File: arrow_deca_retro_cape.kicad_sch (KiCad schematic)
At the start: 26 parts, among them J1 ZXSP_ED2X28_SPE_SOL_EDGE, J10 Conn_02x05_Odd_Even, J12 Conn_01x03, J13 Conn_01x01, J14 Conn_01x02, J15 Conn_01x03, J16 Conn_01x06, J2 Conn_01x03, J4 DB9_Male, J5 DINC_MIN_TM_6_1, J6 Conn_02x20_Odd_Even, J7 Conn_01x03, J8 P8_Male, J9 P9_Male, U4 LM1117-3.3, U5 LM1117-2.5

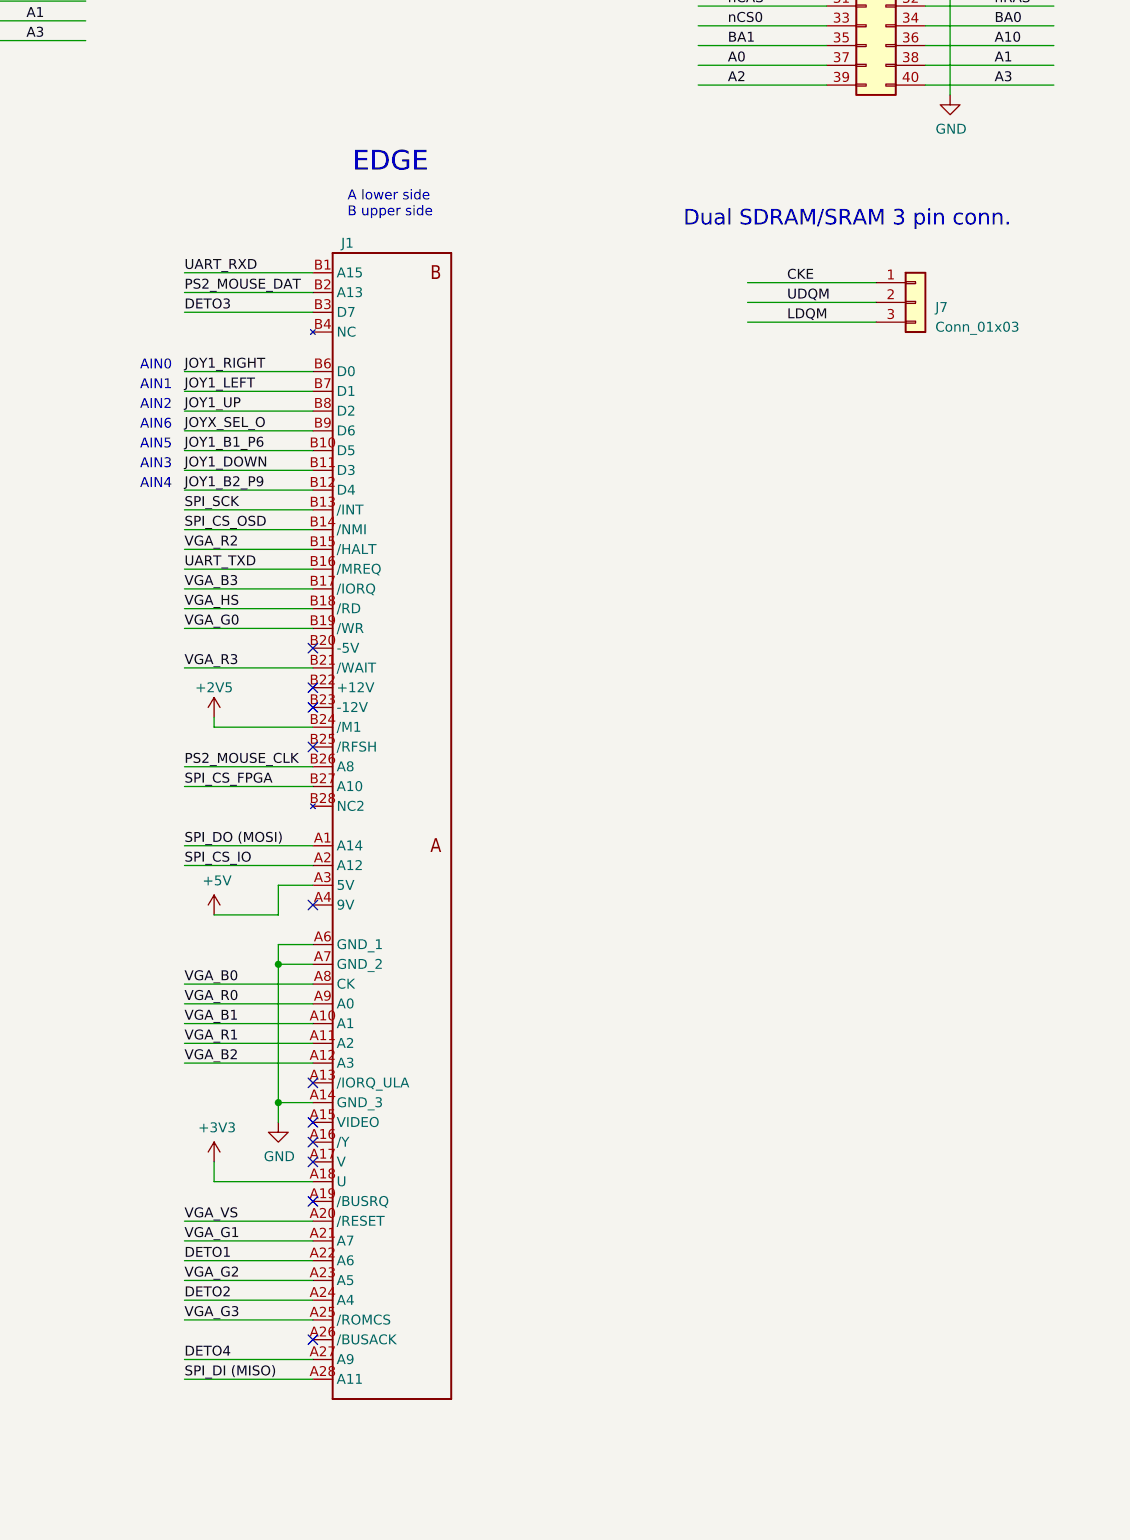
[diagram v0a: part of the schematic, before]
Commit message: v0.61 2-layer. Edge removed
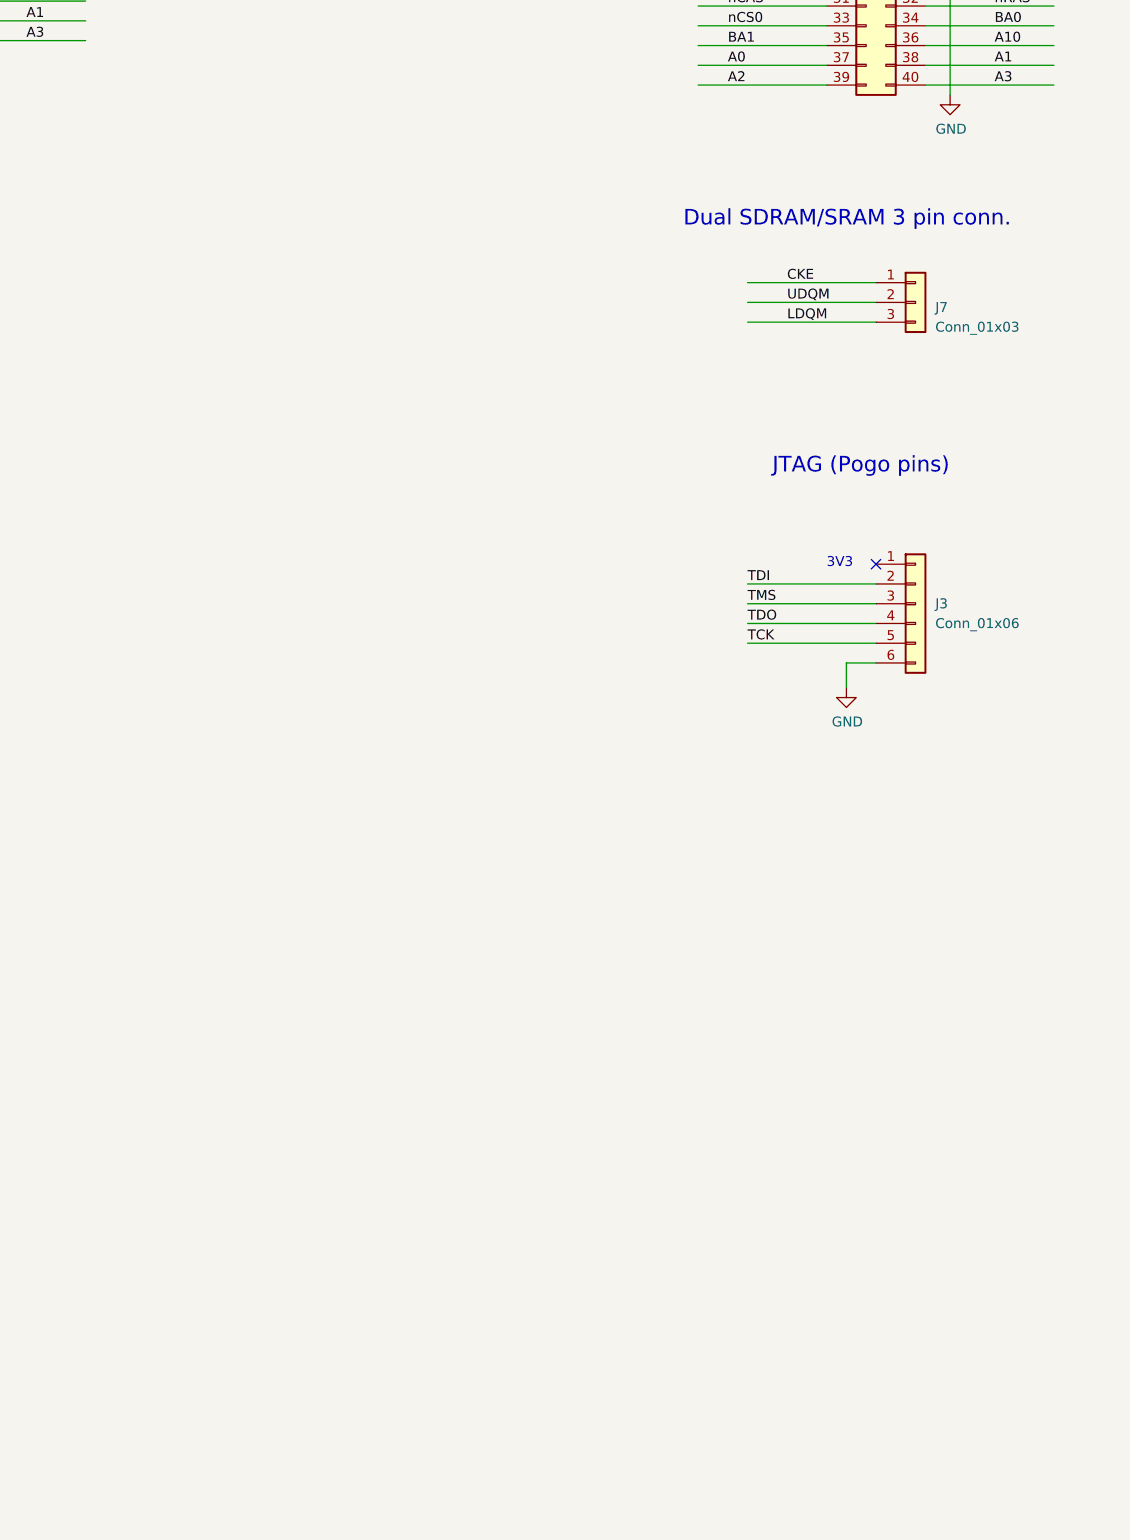
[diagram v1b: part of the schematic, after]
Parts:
- removed J1: ZXSP_ED2X28_SPE_SOL_EDGE, addon-edge-rpi-i2s-pmod:2X28_SPE2, symbol gomaDOSzero-eagle-import:ZXSP_ED2X28_SPE_SOL_EDGE
- added J3: Conn_01x06, Connector_PinHeader_2.54mm:PinHeader_1x06_P2.54mm_Vertical, symbol Connector_Generic:Conn_01x06
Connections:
- net GND: now also J3.6 (Pin_6)
- new net TCK: J3.5 (Pin_5)
- new net TDI: J3.2 (Pin_2)
- new net TDO: J3.4 (Pin_4)
- new net TMS: J3.3 (Pin_3)
- no-connect marks 13 -> 3
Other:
- note added: "3V3"
- note added: "JTAG (Pogo pins)"
- note removed: "A lower side B upper side"
- note removed: "EDGE"

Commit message: v0.62 only vga routing missing
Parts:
- removed J4: DB9_Male, Connector_Dsub:DSUB-9_Male_Horizontal_P2.77x2.84mm_EdgePinOffset9.90mm_Housed_MountingHolesOffset11.32mm, symbol Connector:DB9_Male
- added D10, D11, D12, D3, D4, D5, D6, D7, D8, D9: BAT54S, Package_TO_SOT_SMD:SOT-23, symbol Diode:BAT54S
- added J1: DB15_Female_HighDensity, vga:DSUB-15-HD_Female_Horizontal_P2.29x2.54mm_EdgePinOffset3.03mm_Housed_MountingHolesOffset4.94mm, symbol Connector:DB15_Female_HighDensity
- added J11: PMOD1, addon-edge-rpi-i2s-pmod:Pmod_2x06_P2.54mm_Vertical_2, symbol Connector_Generic:Conn_02x06_Top_Bottom
- added J12: PMOD2, addon-edge-rpi-i2s-pmod:Pmod_2x06_P2.54mm_Vertical_2, symbol Connector_Generic:Conn_02x06_Top_Bottom
- added J17: Conn_01x02, Connector_PinSocket_2.54mm:PinSocket_1x02_P2.54mm_Vertical, symbol Connector_Generic:Conn_01x02
- added J19: DINC_MIN_TM_6_1, ps2:DINC_MIN_TM_6_1PRIMARY, symbol zxuno-eagle-import:DINC_MIN_TM_6_1
- added J20: PMOD3, addon-edge-rpi-i2s-pmod:PMOD_Female_Horizontal_2, symbol Connector_Generic:Conn_02x06_Top_Bottom
- added J21: USB3_A, Connector_USB:USB3_A_Molex_48393-001, symbol Connector:USB3_A
- added J22: Conn_01x03, Connector_PinHeader_2.54mm:PinHeader_1x03_P2.54mm_Vertical, symbol Connector_Generic:Conn_01x03
- added J4: DB9_Male_MountingHoles, Connector_Dsub:DSUB-9_Male_Horizontal_P2.77x2.84mm_EdgePinOffset9.90mm_Housed_MountingHolesOffset11.32mm, symbol Connector:DB9_Male_MountingHoles
- added JP1: Conn_01x02, Connector_PinHeader_2.54mm:PinHeader_1x02_P2.54mm_Vertical, symbol Connector_Generic:Conn_01x02
- added R10, R11, R12, R13, R14, R15, R16, R9: 100, Resistor_SMD:R_0805_2012Metric_Pad1.20x1.40mm_HandSolder, symbol Device:R
- added R5, R6: 120, Resistor_SMD:R_0805_2012Metric_Pad1.20x1.40mm_HandSolder, symbol Device:R
- added R7, R8: DNI, Resistor_SMD:R_0805_2012Metric_Pad1.20x1.40mm_HandSolder, symbol Device:R
- R1, R2: value 120 -> 100
- R3, R4: value NC -> DNI
- renumbered J12 to J18
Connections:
- net +2V5: now also D10.2, D11.2, D12.2, D5.2, D6.2, D7.2, D8.2, D9.2
- net +3V3: now also D3.2, D4.2, J11.12 (Pin_12), J11.6 (Pin_6), J12.12 (Pin_12), J12.6 (Pin_6), J22.3 (Pin_3), JP1.1 (Pin_1)
- net +5V: now also J17.1 (Pin_1), J19.4, J21.1 (VBUS), J4.5
- net DETO1: now also J12.9 (Pin_9)
- net DETO2: now also J12.10 (Pin_10)
- net GND: now also D10.1, D11.1, D12.1, D3.1, D4.1, D5.1, D6.1, D7.1, D8.1, D9.1, J1.10, J1.5, J1.6, J1.7, J1.8, J11.11 (Pin_11), J11.5 (Pin_5), J12.11 (Pin_11), J12.5 (Pin_5), J17.2 (Pin_2), J19.3, J20.11 (Pin_11), J20.5 (Pin_5), J21.10 (SHIELD), J21.4 (GND), J4.8, R7.2, R8.2
- net JOY1_B1_P6: now also R14.1
- net JOY1_B2_P9: now also R9.1
- net JOY1_DOWN: now also R13.1
- net JOY1_LEFT: now also R11.1
- net JOY1_RIGHT: now also R10.1
- net JOY1_UP: now also R15.1
- net JOYX_SEL_O: now also R12.1
- net PS2_MOUSE_CLK: now also R5.1
- net PS2_MOUSE_DAT: now also R6.1
- net SPI_CS_FPGA: now also J20.10 (Pin_10)
- net SPI_CS_IO: now also J20.9 (Pin_9)
- net SPI_CS_OSD: now also J20.1 (Pin_1)
- net SPI_DI (MISO): now also J20.3 (Pin_3)
- net SPI_DO (MOSI): now also J20.2 (Pin_2)
- net SPI_SCK: now also J20.4 (Pin_4)
- net UART_RXD: now also J20.7 (Pin_7)
- net UART_TXD: now also J20.8 (Pin_8)
- net VGA_B0: now also J11.7 (Pin_7)
- net VGA_B1: now also J11.8 (Pin_8)
- net VGA_B2: now also J11.9 (Pin_9)
- net VGA_B3: now also J11.10 (Pin_10)
- net VGA_G0: now also J12.1 (Pin_1)
- net VGA_G1: now also J12.2 (Pin_2)
- net VGA_G2: now also J12.3 (Pin_3)
- net VGA_G3: now also J12.4 (Pin_4)
- net VGA_HS: now also J12.7 (Pin_7)
- net VGA_R0: now also J11.1 (Pin_1)
- net VGA_R1: now also J11.2 (Pin_2)
- net VGA_R2: now also J11.3 (Pin_3)
- net VGA_R3: now also J11.4 (Pin_4)
- net VGA_VS: now also J12.8 (Pin_8)
- net DETO3 renamed JOY_MUX_DETO3
- net JOY_MUX_DETO3: now also R16.1
- new net: D3.3, J19.1, R6.2, R7.1
- new net: D5.3, J22.1 (Pin_1), R9.2
- new net: D4.3, J19.5, R5.2, R8.1
- new net D+: D6.3, J21.3 (D+), J4.2, R13.2
- new net D-: D10.3, J21.2 (D-), J4.1, R15.2
- new net DRAIN: D7.3, J21.7 (DRAIN), J4.4, R10.2
- new net MUX: D12.3, J4.0 (PAD), R16.2
- new net RX+: D11.3, J21.6 (SSRX+), J4.7, R12.2
- new net RX-: D9.3, J21.5 (SSRX-), J4.3, R11.2
- new net TX+: J21.9 (SSTX+), J22.2 (Pin_2), J4.9
- new net TX-: D8.3, J21.8 (SSTX-), J4.6, R14.2
- new net VGA222_HS: J1.13
- new net VGA222_VS: J1.14
- new net VGAB: J1.3
- new net VGAG: J1.2
- new net VGAR: J1.1
- new net VH_PMOD: J20.12 (Pin_12), J20.6 (Pin_6), JP1.2 (Pin_2)
- no-connect marks 3 -> 10
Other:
- note added: "-R2R VGA - REVISAR PINOUT, i2s retorn deca a DAC DETO 2, 3, 4 - I2S header al DETO PMOD"
- note added: "Central +5V"
- note added: "Mini-DIN 6P - PS2 KEYBOARD"
- note added: "Mini-DIN 6P - PS2 MOUSE"
- note added: "PMOD 1"
- note added: "PMOD 2"
- note added: "PMOD 3 (SPI+UART)"
- note added: "USB3 USER PORT"
- note added: "VGA"
- note removed: "- REVISAR PINOUT, i2s retorn deca a DAC DETO 2, 3, 4 - USB3 SERIAL - I2S header al DETO PMOD - PS2 MOUSE connector - PULL DOWN PS2 GND POSAR A SORTIDES FPGA - REVISAR PULL DOWN CKE"
- note removed: "Mini-DIN 6P - PS2 Connector"
- moved on the sheet: C18, C19, C20, C21, D1, D2, J10, J13, J14, J15, J16, J18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

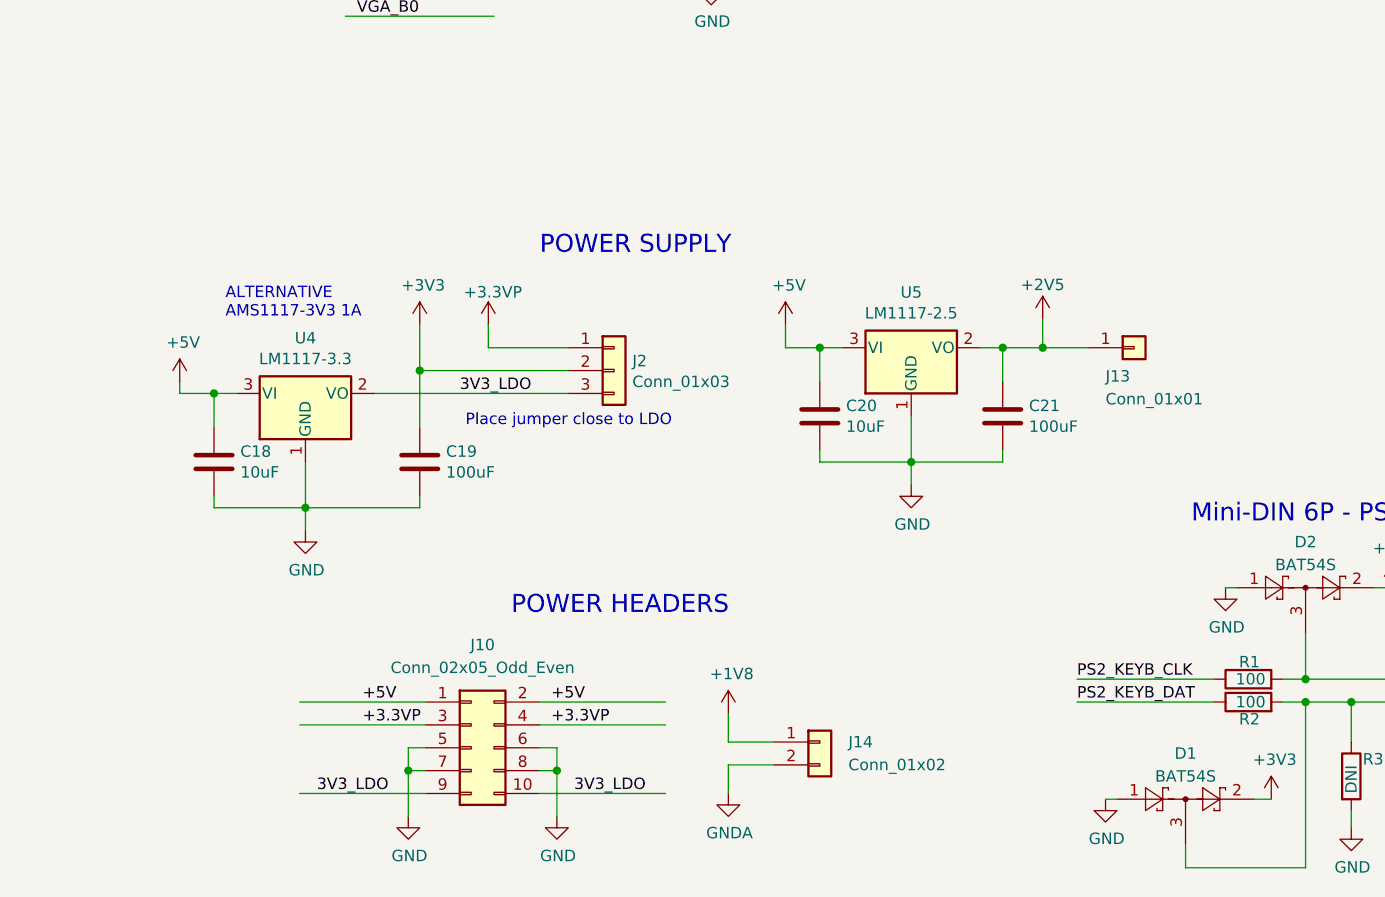
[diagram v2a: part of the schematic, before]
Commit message: v0.62 final without vga
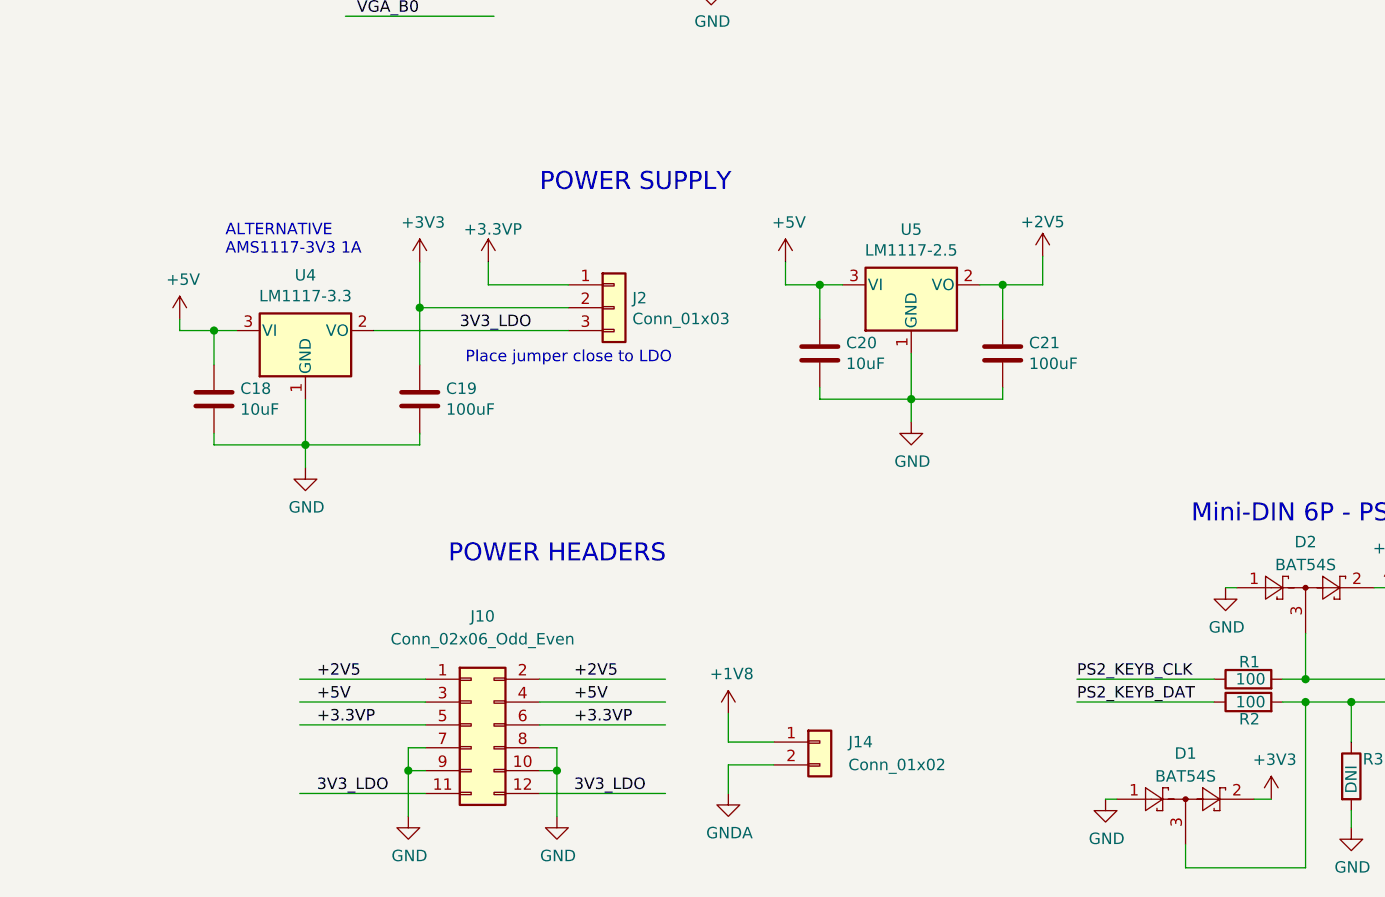
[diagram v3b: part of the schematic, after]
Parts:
- removed J10: Conn_02x05_Odd_Even, Connector_PinSocket_2.54mm:PinSocket_2x05_P2.54mm_Vertical, symbol Connector_Generic:Conn_02x05_Odd_Even
- removed J13: Conn_01x01, Connector_PinSocket_2.54mm:PinSocket_1x01_P2.54mm_Vertical, symbol Connector_Generic:Conn_01x01
- added J10: Conn_02x06_Odd_Even, Connector_PinSocket_2.54mm:PinSocket_2x06_P2.54mm_Vertical, symbol Connector_Generic:Conn_02x06_Odd_Even
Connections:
- net +2V5: now also J10.1 (Pin_1), J10.2 (Pin_2)
- net +3.3VP: now also J10.5 (Pin_5), J10.6 (Pin_6)
- net +5V: now also J10.3 (Pin_3), J10.4 (Pin_4)
- net 3V3_LDO: now also J10.11 (Pin_11), J10.12 (Pin_12)
- net GND: now also J10.10 (Pin_10), J10.7 (Pin_7), J10.8 (Pin_8), J10.9 (Pin_9)
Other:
- moved on the sheet: C18, C19, C20, C21, J2, U4, U5

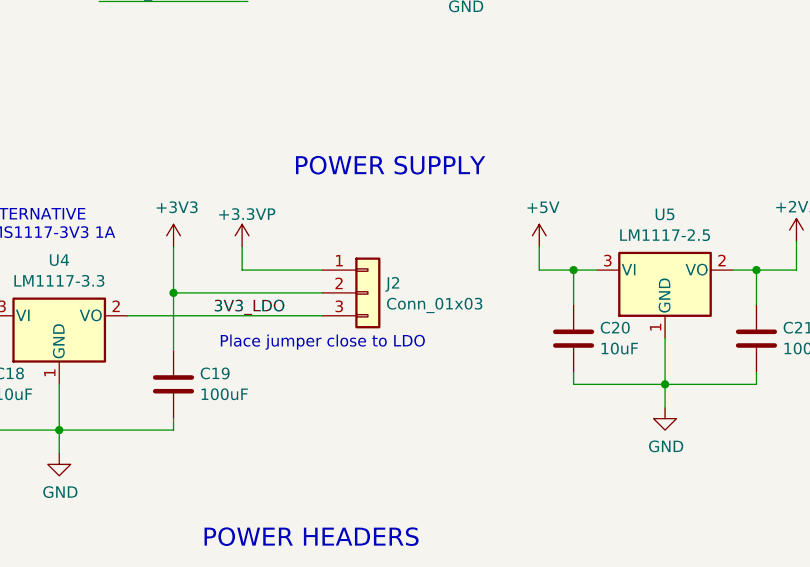
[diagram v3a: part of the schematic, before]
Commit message: v0.65 power header changed
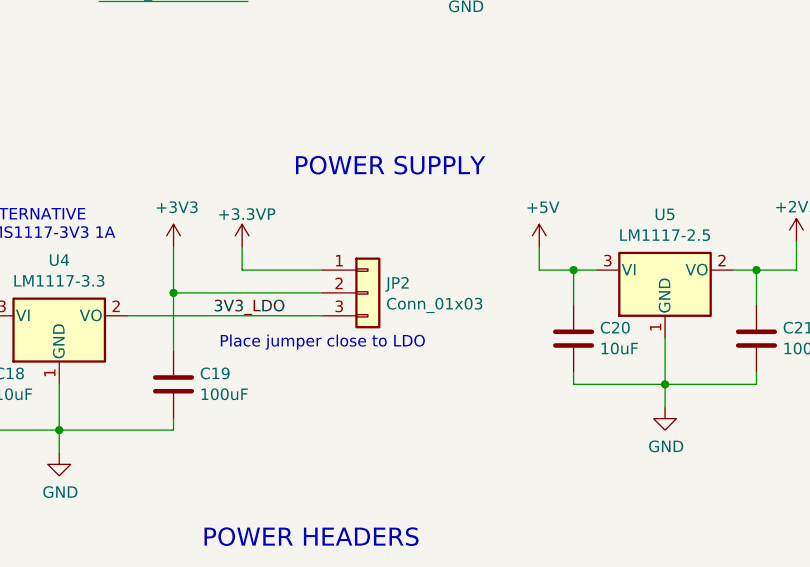
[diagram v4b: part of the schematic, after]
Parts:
- renumbered J2 to JP2
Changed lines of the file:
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@@
   (symbol (lib_id "Connector_Generic:Conn_01x03") (at 64.135 218.44 0) (unit 1)
     (in_bom yes) (on_board yes)
-    (property "Reference" "J2" (id 0) (at 66.167 217.3732 0)
+    (property "Reference" "JP2" (id 0) (at 66.167 217.3732 0)
       (effects (font (size 1.27 1.27)) (justify left))
     )
@@
       (reference "J1") (unit 1) (value "DB15_Female_HighDensity") (footprint "vga:DSUB-15-HD_Female_Horizontal_P2.29x2.54mm_EdgePinOffset3.03mm_Housed_MountingHolesOffset4.94mm")
     )
-    (path "/00000000-0000-0000-0000-000061199143"
-      (reference "J2") (unit 1) (value "Conn_01x03") (footprint "Connector_PinHeader_2.54mm:PinHeader_1x03_P2.54mm_Vertical")
-    )
     (path "/e9a4ad61-c16f-4a36-9385-12858092576f"
       (reference "J3") (unit 1) (value "Conn_01x06") (footprint "Connector_PinHeader_2.54mm:PinHeader_1x06_P2.54mm_Vertical")
@@
       (reference "JP1") (unit 1) (value "Conn_01x02") (footprint "Connector_PinHeader_2.54mm:PinHeader_1x02_P2.54mm_Vertical")
     )
+    (path "/00000000-0000-0000-0000-000061199143"
+      (reference "JP2") (unit 1) (value "Conn_01x03") (footprint "Connector_PinHeader_2.54mm:PinHeader_1x03_P2.54mm_Vertical")
+    )
     (path "/439aafdc-2c0e-44db-ab96-7212e6daa700"
